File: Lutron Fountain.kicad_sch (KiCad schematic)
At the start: 0 parts

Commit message: commit two
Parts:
- added D1, D3, D5, D7: 1N4148, Diode_THT:D_DO-35_SOD27_P7.62mm_Horizontal, symbol Diode:1N4148
- added D10, D2, D4, D6, D8: LED, symbol Device:LED
- added Q1, Q2, Q3, Q4, Q5: BC547, Package_TO_SOT_THT:TO-92_Inline, symbol Transistor_BJT:BC547
- added R1, R3, R5, R7, R9: 10k, symbol Device:R
- added R10, R2, R4, R6, R8: 220, symbol Device:R
- added RV1: R_Potentiometer, symbol Device:R_Potentiometer
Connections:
- new net: D10.1 (K), Q5.1 (C)
- new net: Q5.2 (B), R9.1
- new net: D6.2 (A), R6.2
- new net: D2.1 (K), Q1.1 (C)
- new net: Q1.2 (B), R1.1
- new net: D5.1 (K), D7.2 (A), R7.2
- new net: D3.1 (K), D5.2 (A), R5.2
- new net: D1.1 (K), D3.2 (A), R3.2
- new net: D1.2 (A), R1.2, RV1.2
- new net: Q3.2 (B), R5.1
- new net: D10.2 (A), R10.2
- new net: D4.1 (K), Q2.1 (C)
- new net: D4.2 (A), R4.2
- new net: D7.1 (K), R9.2
- new net: D8.1 (K), Q4.1 (C)
- new net: Q4.2 (B), R7.1
- new net: D8.2 (A), R8.2
- new net: D2.2 (A), R2.2
- new net: D6.1 (K), Q3.1 (C)
- new net: Q2.2 (B), R3.1
- new net +5V: R10.1, R2.1, R4.1, R6.1, R8.1, RV1.1
- new net GND: Q1.3 (E), Q2.3 (E), Q3.3 (E), Q4.3 (E), Q5.3 (E), RV1.3

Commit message: addition three
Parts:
- added D11, D13, D15, D17, D18: LED, symbol Device:LED
- added D12, D14, D16, D9: 1N4148, Diode_THT:D_DO-35_SOD27_P7.62mm_Horizontal, symbol Diode:1N4148
- added Q10, Q6, Q7, Q8, Q9: BC547, Package_TO_SOT_THT:TO-92_Inline, symbol Transistor_BJT:BC547
- added R11, R13, R15, R17, R19: 10k, symbol Device:R
- added R12, R14, R16, R18, R20: 220, symbol Device:R
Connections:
- net +5V: now also R12.1, R14.1, R16.1, R18.1, R20.1
- net GND: now also Q10.3 (E), Q6.3 (E), Q7.3 (E), Q8.3 (E), Q9.3 (E)
- net at D1.2 (A), R1.2, RV1.2: now also D9.2 (A), R11.2
- new net: D13.2 (A), R14.2
- new net: Q9.2 (B), R17.1
- new net: D14.1 (K), D16.2 (A), R17.2
- new net: D12.1 (K), D14.2 (A), R15.2
- new net: D12.2 (A), D9.1 (K), R13.2
- new net: D15.1 (K), Q8.1 (C)
- new net: D15.2 (A), R16.2
- new net: D17.1 (K), Q9.1 (C)
- new net: D17.2 (A), R18.2
- new net: Q8.2 (B), R15.1
- new net: Q10.2 (B), R19.1
- new net: D16.1 (K), R19.2
- new net: D13.1 (K), Q7.1 (C)
- new net: D11.1 (K), Q6.1 (C)
- new net: Q6.2 (B), R11.1
- new net: D18.2 (A), R20.2
- new net: Q7.2 (B), R13.1
- new net: D11.2 (A), R12.2
- new net: D18.1 (K), Q10.1 (C)
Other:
- company: (none) -> Anna Tretiakova
- title: (none) -> Lutron Competition Fountain

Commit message: schematic done
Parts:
- added D19, D20, D23, D24, D27, D28, D31, D32: 1N4148, Diode_THT:D_DO-35_SOD27_P7.62mm_Horizontal, symbol Diode:1N4148
- added D21, D22, D25, D26, D29, D30, D33, D34, D35, D36: RLED, LED_THT:LED_D5.0mm, symbol Device:LED
- added Q11, Q12, Q13, Q14, Q15, Q16, Q17, Q18, Q19, Q20: BC547, Package_TO_SOT_THT:TO-92_Inline, symbol Transistor_BJT:BC547
- added R21, R22, R25, R26, R29, R30, R33, R34, R37, R38: 10k, Resistor_THT:R_Axial_DIN0207_L6.3mm_D2.5mm_P7.62mm_Horizontal, symbol Device:R
- added R23, R24, R27, R28, R31, R32, R35, R36, R39, R40: 220, Resistor_THT:R_Axial_DIN0207_L6.3mm_D2.5mm_P7.62mm_Horizontal, symbol Device:R
- added RV2: R_Potentiometer, Potentiometer_THT:Potentiometer_Bourns_3386F_Vertical, symbol Device:R_Potentiometer
- D10, D11, D13, D15, D17, D18, D2, D4, D6, D8: value LED -> RLED; footprint (none) -> LED_THT:LED_D5.0mm
- R1, R10, R11, R12, R13, R14, R15, R16, R17, R18, R19, R2, R20, R3, R4, R5, R6, R7, R8, R9: footprint (none) -> Resistor_THT:R_Axial_DIN0207_L6.3mm_D2.5mm_P7.62mm_Horizontal
- RV1: footprint (none) -> Potentiometer_THT:Potentiometer_Bourns_3386F_Vertical
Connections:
- net +5V: now also R23.1, R24.1, R27.1, R28.1, R31.1, R32.1, R35.1, R36.1, R39.1, R40.1, RV2.1
- net GND: now also Q11.3 (E), Q12.3 (E), Q13.3 (E), Q14.3 (E), Q15.3 (E), Q16.3 (E), Q17.3 (E), Q18.3 (E), Q19.3 (E), Q20.3 (E), RV2.3
- new net: Q17.2 (B), R33.1
- new net: D27.1 (K), D31.2 (A), R33.2
- new net: D21.1 (K), Q11.1 (C)
- new net: Q11.2 (B), R21.1
- new net: D30.1 (K), Q16.1 (C)
- new net: Q16.2 (B), R30.1
- new net: D23.1 (K), D27.2 (A), R29.2
- new net: D33.1 (K), Q17.1 (C)
- new net: D33.2 (A), R35.2
- new net: D24.1 (K), D28.2 (A), R30.2
- new net: D25.1 (K), Q13.1 (C)
- new net: Q13.2 (B), R25.1
- new net: D21.2 (A), R23.2
- new net: D22.2 (A), R24.2
- new net: D36.2 (A), R40.2
- new net: D19.1 (K), D23.2 (A), R25.2
- new net: D34.1 (K), Q18.1 (C)
- new net: Q18.2 (B), R34.1
- new net: D31.1 (K), R37.2
- new net: D20.1 (K), D24.2 (A), R26.2
- new net: D19.2 (A), D20.2 (A), R21.2, R22.2, RV2.2
- new net: D34.2 (A), R36.2
- new net: D29.2 (A), R31.2
- new net: D36.1 (K), Q20.1 (C)
- new net: Q12.2 (B), R22.1
- new net: D26.2 (A), R28.2
- new net: D25.2 (A), R27.2
- new net: D22.1 (K), Q12.1 (C)
- new net: Q14.2 (B), R26.1
- new net: Q15.2 (B), R29.1
- new net: Q20.2 (B), R38.1
- new net: D28.1 (K), D32.2 (A), R34.2
- new net: D35.1 (K), Q19.1 (C)
- new net: D35.2 (A), R39.2
- new net: D29.1 (K), Q15.1 (C)
- new net: Q19.2 (B), R37.1
- new net: D30.2 (A), R32.2
- new net: D26.1 (K), Q14.1 (C)
- new net: D32.1 (K), R38.2
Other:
- moved on the sheet: D1, D10, D11, D12, D13, D14, D15, D16, D17, D18, D2, D3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

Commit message: pcb finished
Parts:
- added J1: Barrel_Jack_MountingPin, Connector_BarrelJack:BarrelJack_CUI_PJ-102AH_Horizontal, symbol Connector:Barrel_Jack_MountingPin
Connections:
- net +5V: now also J1.1
- net GND: now also J1.2
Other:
- moved on the sheet: D1, D10, D11, D12, D13, D14, D15, D16, D17, D18, D19, D2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

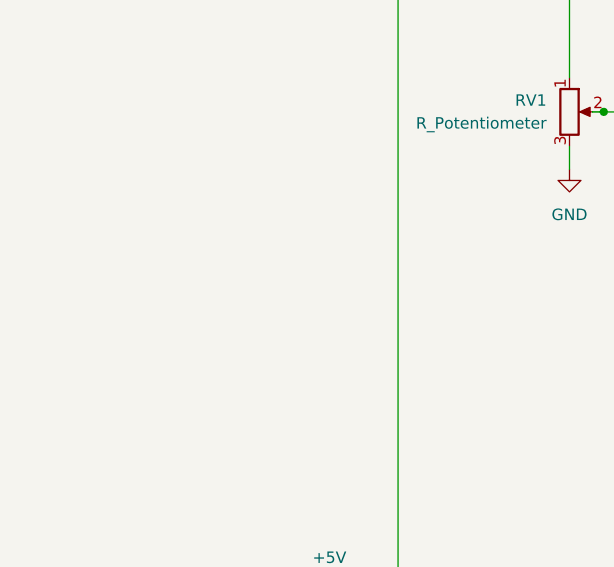
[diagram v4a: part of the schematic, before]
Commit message: added gnd and power
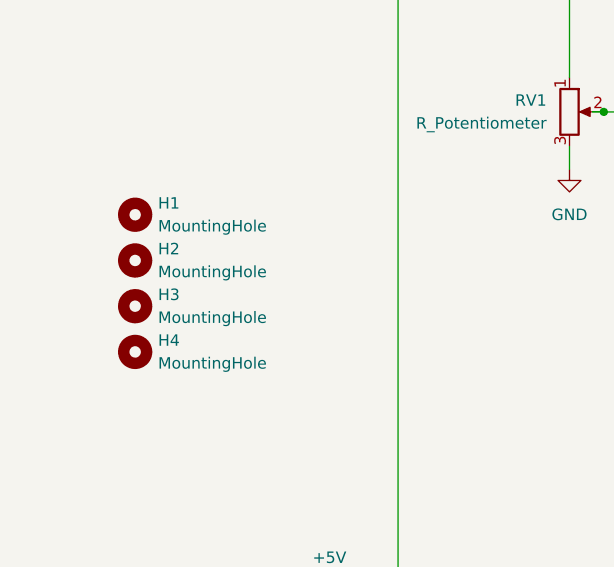
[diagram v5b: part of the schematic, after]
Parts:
- added H1, H2, H3, H4: MountingHole, MountingHole:MountingHole_4.3mm_M4_Pad, symbol Mechanical:MountingHole

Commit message: finalized
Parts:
- removed D10, D11, D13, D15, D17, D18, D2, D21, D22, D25, D26, D29, D30, D33, D34, D35, D36, D4, D6, D8: RLED, LED_THT:LED_D5.0mm, symbol Device:LED
- removed J1: Barrel_Jack_MountingPin, Connector_BarrelJack:BarrelJack_CUI_PJ-102AH_Horizontal, symbol Connector:Barrel_Jack_MountingPin
- added J1: Power, TerminalBlock:TerminalBlock_MaiXu_MX126-5.0-02P_1x02_P5.00mm, symbol Connector:Screw_Terminal_01x02
- added J10, J11, J12, J13, J14, J15, J16, J17, J18, J19, J2, J20, J21, J3, J4, J5, J6, J7, J8, J9: LED, TerminalBlock:TerminalBlock_MaiXu_MX126-5.0-02P_1x02_P5.00mm, symbol Connector:Screw_Terminal_01x02
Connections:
- net +5V: now also J1.2 (Pin_2)
- net GND: now also J1.1 (Pin_1)
- net at Q5.1 (C): now also J6.2 (Pin_2)
- net at Q11.1 (C): now also J12.2 (Pin_2)
- net at R6.2: now also J4.1 (Pin_1)
- net at Q16.1 (C): now also J19.1 (Pin_1)
- net at Q17.1 (C): now also J15.2 (Pin_2)
- net at R35.2: now also J15.1 (Pin_1)
- net at Q1.1 (C): now also J2.2 (Pin_2)
- net at R14.2: now also J8.2 (Pin_2)
- net at Q13.1 (C): now also J13.2 (Pin_2)
- net at R23.2: now also J12.1 (Pin_1)
- net at R24.2: now also J17.2 (Pin_2)
- net at R40.2: now also J21.2 (Pin_2)
- net at R10.2: now also J6.1 (Pin_1)
- net at Q8.1 (C): now also J9.1 (Pin_1)
- net at R16.2: now also J9.2 (Pin_2)
- net at Q9.1 (C): now also J10.1 (Pin_1)
- net at R18.2: now also J10.2 (Pin_2)
- net at Q18.1 (C): now also J20.1 (Pin_1)
- net at R36.2: now also J20.2 (Pin_2)
- net at Q2.1 (C): now also J3.2 (Pin_2)
- net at R4.2: now also J3.1 (Pin_1)
- net at R31.2: now also J14.1 (Pin_1)
- net at Q20.1 (C): now also J21.1 (Pin_1)
- net at R28.2: now also J18.2 (Pin_2)
- net at R27.2: now also J13.1 (Pin_1)
- net at Q12.1 (C): now also J17.1 (Pin_1)
- net at Q7.1 (C): now also J8.1 (Pin_1)
- net at Q6.1 (C): now also J7.1 (Pin_1)
- net at R20.2: now also J11.2 (Pin_2)
- net at Q4.1 (C): now also J5.2 (Pin_2)
- net at R8.2: now also J5.1 (Pin_1)
- net at Q19.1 (C): now also J16.2 (Pin_2)
- net at R39.2: now also J16.1 (Pin_1)
- net at Q15.1 (C): now also J14.2 (Pin_2)
- net at R12.2: now also J7.2 (Pin_2)
- net at Q10.1 (C): now also J11.1 (Pin_1)
- net at R32.2: now also J19.2 (Pin_2)
- net at R2.2: now also J2.1 (Pin_1)
- net at Q14.1 (C): now also J18.1 (Pin_1)
- net at Q3.1 (C): now also J4.2 (Pin_2)
